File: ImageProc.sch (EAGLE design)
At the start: 96 parts, among them IC1 XC61GC3002HR-G, IC2 MIC5335-SPYMT, IC3 LTC6087, IC4 LTC6087, IC5 AT86RF233-ZU, IC7 DRV8833RTY, IC8 DRV8833RTY, IC9 MPU-6000, J1 CON-HRS-DM3AT, P1 BAT+, P10 MD2, P2 BAT-, P3 MA1, P4 MA2, P5 MB1, P6 MB2, P7 MC1, P8 MC2, P9 MD1, U1 CY8C5688LTI-LP086, U2 SIT8008AI-72-33E-24.000000G

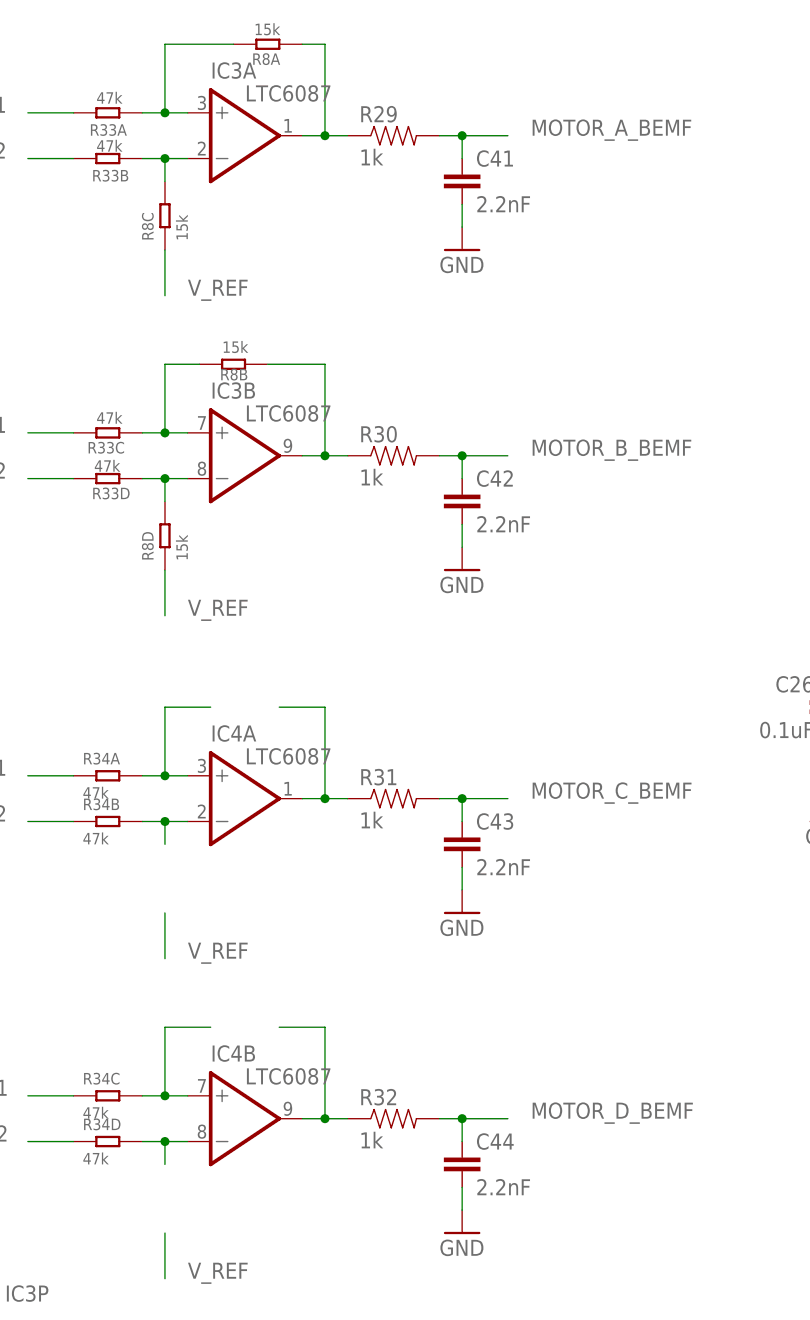
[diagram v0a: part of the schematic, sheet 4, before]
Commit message: Further routing. Moved 1K resistors to res array.
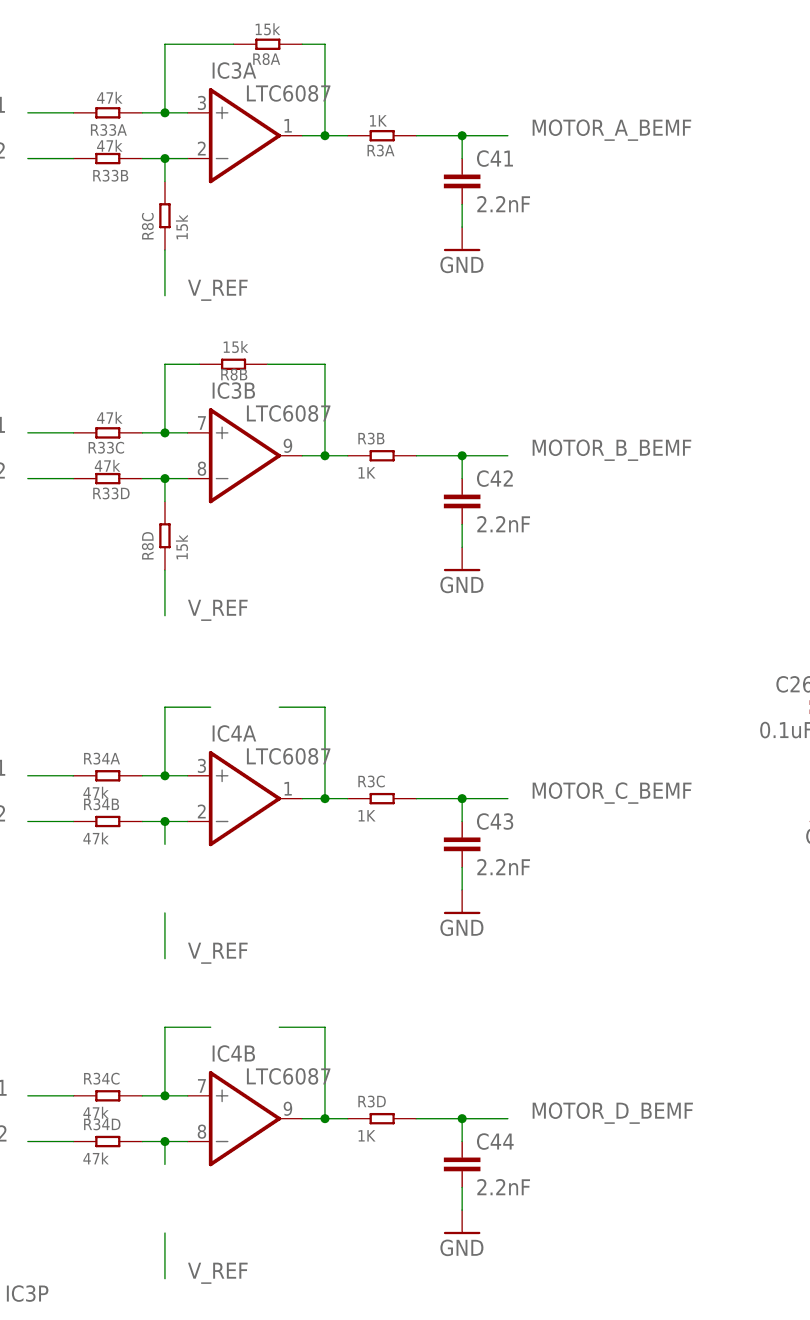
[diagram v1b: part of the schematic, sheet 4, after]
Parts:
- removed R29, R30, R31, R32: 1k, biomimetic:RESISTOR0402-RES
- added R3: 1K, OPL Eagle Library:R-4R
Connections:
- removed net N$21: R4.1, U1G$6.SCL1
- net MOTOR_A_BEMF: now also R3A.2; no longer R29.2
- net MOTOR_B_BEMF: now also R3B.2; no longer R30.2
- net MOTOR_C_BEMF: now also R3C.2; no longer R31.2
- net MOTOR_D_BEMF: now also R3D.2; no longer R32.2
- net N$34: now also R3D.1; no longer R32.1
- net N$35: now also R3C.1; no longer R31.1
- net N$36: now also R3A.1; no longer R29.1
- net N$37: now also R3B.1; no longer R30.1
- net SCL1: now also R4.1, U1G$6.SCL1
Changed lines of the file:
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@@
 <part name="C26" library="biomimetic" deviceset="CAP" device="0402-CAP" value="0.1uF"/>
 <part name="C41" library="biomimetic" deviceset="CAP" device="0402-CAP" value="2.2nF"/>
-<part name="R29" library="biomimetic" deviceset="RESISTOR" device="0402-RES" value="1k"/>
 <part name="C42" library="biomimetic" deviceset="CAP" device="0402-CAP" value="2.2nF"/>
-<part name="R30" library="biomimetic" deviceset="RESISTOR" device="0402-RES" value="1k"/>
 <part name="C43" library="biomimetic" deviceset="CAP" device="0402-CAP" value="2.2nF"/>
-<part name="R31" library="biomimetic" deviceset="RESISTOR" device="0402-RES" value="1k"/>
 <part name="C44" library="biomimetic" deviceset="CAP" device="0402-CAP" value="2.2nF"/>
-<part name="R32" library="biomimetic" deviceset="RESISTOR" device="0402-RES" value="1k"/>
 <part name="GND20" library="biomimetic" deviceset="GND" device=""/>
 <part name="GND26" library="biomimetic" deviceset="GND" device=""/>
@@
 <part name="C40" library="biomimetic" deviceset="CAP" device="0402-CAP" value="1.0uF"/>
 <part name="GND11" library="supply1" deviceset="GND" device=""/>
-<part name="P+10" library="biomimetic" deviceset="3.3V" device=""/>
-<part name="P+5" library="biomimetic" deviceset="3.3V" device=""/>
-<part name="P+7" library="biomimetic" deviceset="3.3V" device=""/>
 <part name="D1" library="diode" deviceset="DIODE-" device="SOD123"/>
 <part name="L1" library="pullin" deviceset="SRN3015-100M" device="" value="10uH"/>
@@
 <part name="GND12" library="supply1" deviceset="GND" device=""/>
 <part name="GND19" library="supply1" deviceset="GND" device=""/>
+<part name="P+5" library="biomimetic" deviceset="3.3V" device=""/>
+<part name="P+7" library="biomimetic" deviceset="3.3V" device=""/>
+<part name="P+10" library="biomimetic" deviceset="3.3V" device=""/>
+<part name="R3" library="OPL Eagle Library" deviceset="R-4R*" device="" value="1K"/>
 </parts>
 <sheets>
@@
 <instance part="C40" gate="G$1" x="119.38" y="22.86"/>
 <instance part="GND11" gate="1" x="101.6" y="55.88"/>
-<instance part="P+10" gate="G$1" x="60.96" y="66.04"/>
-<instance part="P+5" gate="G$1" x="68.58" y="66.04"/>
-<instance part="P+7" gate="G$1" x="76.2" y="66.04"/>
 <instance part="U2" gate="G$1" x="193.04" y="162.56"/>
 <instance part="C48" gate="G$1" x="210.82" y="162.56" rot="MR0">
@@
 <instance part="P+9" gate="G$1" x="175.26" y="170.18"/>
 <instance part="GND12" gate="1" x="167.64" y="154.94"/>
+<instance part="P+5" gate="G$1" x="76.2" y="66.04"/>
+<instance part="P+7" gate="G$1" x="68.58" y="66.04"/>
+<instance part="P+10" gate="G$1" x="60.96" y="66.04"/>
 </instances>
 <busses>
@@
 <wire x1="66.04" y1="162.56" x2="68.58" y2="162.56" width="0.1524" layer="91"/>
 <junction x="66.04" y="170.18"/>
-</segment>
-<segment>
-<wire x1="60.96" y1="66.04" x2="60.96" y2="55.88" width="0.1524" layer="91"/>
-<pinref part="P+10" gate="G$1" pin="3.3V"/>
-</segment>
-<segment>
-<wire x1="68.58" y1="66.04" x2="68.58" y2="55.88" width="0.1524" layer="91"/>
-<pinref part="P+5" gate="G$1" pin="3.3V"/>
-</segment>
-<segment>
-<wire x1="76.2" y1="66.04" x2="76.2" y2="55.88" width="0.1524" layer="91"/>
-<pinref part="P+7" gate="G$1" pin="3.3V"/>
 </segment>
 <segment>
@@
 <wire x1="167.64" y1="165.1" x2="175.26" y2="165.1" width="0.1524" layer="91"/>
 <junction x="175.26" y="165.1"/>
+</segment>
+<segment>
+<wire x1="76.2" y1="55.88" x2="76.2" y2="66.04" width="0.1524" layer="91"/>
+<pinref part="P+5" gate="G$1" pin="3.3V"/>
+</segment>
+<segment>
+<wire x1="68.58" y1="55.88" x2="68.58" y2="66.04" width="0.1524" layer="91"/>
+<pinref part="P+7" gate="G$1" pin="3.3V"/>
+</segment>
+<segment>
+<wire x1="60.96" y1="55.88" x2="60.96" y2="66.04" width="0.1524" layer="91"/>
+<pinref part="P+10" gate="G$1" pin="3.3V"/>
 </segment>
 </net>
@@
 </segment>
 </net>
-<net name="N$21" class="0">
+<net name="SCL1" class="0">
 <segment>
 <pinref part="R4" gate="G$1" pin="1"/>
@@
 <instance part="C26" gate="G$1" x="220.98" y="104.14" rot="MR0"/>
 <instance part="C41" gate="G$1" x="180.34" y="162.56"/>
-<instance part="R29" gate="G$1" x="172.72" y="167.64"/>
 <instance part="C42" gate="G$1" x="180.34" y="127"/>
-<instance part="R30" gate="G$1" x="172.72" y="132.08"/>
 <instance part="C43" gate="G$1" x="180.34" y="88.9"/>
-<instance part="R31" gate="G$1" x="172.72" y="93.98"/>
 <instance part="C44" gate="G$1" x="180.34" y="53.34"/>
-<instance part="R32" gate="G$1" x="172.72" y="58.42"/>
 <instance part="GND20" gate="1" x="180.34" y="81.28"/>
 <instance part="GND26" gate="1" x="180.34" y="154.94"/>
@@
 <instance part="R8" gate="C" x="147.32" y="158.75" rot="R90"/>
 <instance part="R8" gate="D" x="147.32" y="123.19" rot="R90"/>
+<instance part="R3" gate="A" x="171.45" y="167.64" smashed="yes">
+<attribute name="NAME" x="169.672" y="165.354" size="1.27" layer="95" ratio="10"/>
+<attribute name="VALUE" x="169.926" y="168.656" size="1.27" layer="96" ratio="10"/>
+</instance>
+<instance part="R3" gate="B" x="171.45" y="132.08"/>
+<instance part="R3" gate="C" x="171.45" y="93.98"/>
+<instance part="R3" gate="D" x="171.45" y="58.42"/>
 </instances>
 <busses>
@@
 <net name="MOTOR_D_BEMF" class="0">
 <segment>
-<pinref part="R32" gate="G$1" pin="2"/>
 <label x="187.96" y="58.42" size="1.778" layer="95"/>
-<wire x1="177.8" y1="58.42" x2="180.34" y2="58.42" width="0.1524" layer="91"/>
+<wire x1="175.26" y1="58.42" x2="180.34" y2="58.42" width="0.1524" layer="91"/>
 <pinref part="C44" gate="G$1" pin="1"/>
 <wire x1="180.34" y1="58.42" x2="185.42" y2="58.42" width="0.1524" layer="91"/>
 <wire x1="180.34" y1="55.88" x2="180.34" y2="58.42" width="0.1524" layer="91"/>
 <junction x="180.34" y="58.42"/>
+<pinref part="R3" gate="D" pin="2"/>
 </segment>
 </net>
@@
 <net name="N$34" class="0">
 <segment>
-<pinref part="R32" gate="G$1" pin="1"/>
 <wire x1="162.56" y1="58.42" x2="165.1" y2="58.42" width="0.1524" layer="91"/>
 <wire x1="165.1" y1="58.42" x2="167.64" y2="58.42" width="0.1524" layer="91"/>
@@
 <junction x="165.1" y="58.42"/>
 <pinref part="IC4" gate="B" pin="OUT"/>
+<pinref part="R3" gate="D" pin="1"/>
 </segment>
 </net>
@@
 <wire x1="160.02" y1="104.14" x2="165.1" y2="104.14" width="0.1524" layer="91"/>
 <wire x1="165.1" y1="104.14" x2="165.1" y2="93.98" width="0.1524" layer="91"/>
-<pinref part="R31" gate="G$1" pin="1"/>
 <wire x1="165.1" y1="93.98" x2="167.64" y2="93.98" width="0.1524" layer="91"/>
 <junction x="165.1" y="93.98"/>
 <pinref part="IC4" gate="A" pin="OUT"/>
+<pinref part="R3" gate="C" pin="1"/>
 </segment>
 </net>
@@
 <wire x1="180.34" y1="93.98" x2="185.42" y2="93.98" width="0.1524" layer="91"/>
 <wire x1="180.34" y1="91.44" x2="180.34" y2="93.98" width="0.1524" layer="91"/>
-<pinref part="R31" gate="G$1" pin="2"/>
-<wire x1="177.8" y1="93.98" x2="180.34" y2="93.98" width="0.1524" layer="91"/>
+<wire x1="175.26" y1="93.98" x2="180.34" y2="93.98" width="0.1524" layer="91"/>
 <junction x="180.34" y="93.98"/>
 <label x="187.96" y="93.98" size="1.778" layer="95"/>
+<pinref part="R3" gate="C" pin="2"/>
 </segment>
 </net>
 <net name="N$37" class="0">
 <segment>
-<pinref part="R30" gate="G$1" pin="1"/>
 <wire x1="162.56" y1="132.08" x2="165.1" y2="132.08" width="0.1524" layer="91"/>
 <wire x1="165.1" y1="132.08" x2="167.64" y2="132.08" width="0.1524" layer="91"/>
@@
 <pinref part="R8" gate="B" pin="2"/>
 <pinref part="IC3" gate="B" pin="OUT"/>
+<pinref part="R3" gate="B" pin="1"/>
 </segment>
 </net>
 <net name="MOTOR_B_BEMF" class="0">
 <segment>
-<pinref part="R30" gate="G$1" pin="2"/>
-<wire x1="177.8" y1="132.08" x2="180.34" y2="132.08" width="0.1524" layer="91"/>
+<wire x1="175.26" y1="132.08" x2="180.34" y2="132.08" width="0.1524" layer="91"/>
 <pinref part="C42" gate="G$1" pin="1"/>
 <wire x1="180.34" y1="132.08" x2="185.42" y2="132.08" width="0.1524" layer="91"/>
@@
 <junction x="180.34" y="132.08"/>
 <label x="187.96" y="132.08" size="1.778" layer="95"/>
+<pinref part="R3" gate="B" pin="2"/>
 </segment>
 </net>
 <net name="N$36" class="0">
 <segment>
-<pinref part="R29" gate="G$1" pin="1"/>
 <wire x1="162.56" y1="167.64" x2="165.1" y2="167.64" width="0.1524" layer="91"/>
 <wire x1="165.1" y1="167.64" x2="167.64" y2="167.64" width="0.1524" layer="91"/>
@@
 <pinref part="R8" gate="A" pin="2"/>
 <pinref part="IC3" gate="A" pin="OUT"/>
+<pinref part="R3" gate="A" pin="1"/>
 </segment>
 </net>
 <net name="MOTOR_A_BEMF" class="0">
 <segment>
-<pinref part="R29" gate="G$1" pin="2"/>
-<wire x1="177.8" y1="167.64" x2="180.34" y2="167.64" width="0.1524" layer="91"/>
+<wire x1="175.26" y1="167.64" x2="180.34" y2="167.64" width="0.1524" layer="91"/>
 <pinref part="C41" gate="G$1" pin="1"/>
 <wire x1="180.34" y1="167.64" x2="185.42" y2="167.64" width="0.1524" layer="91"/>
@@
 <junction x="180.34" y="167.64"/>
 <label x="187.96" y="167.64" size="1.778" layer="95"/>
-</segment>
-</net>
+<pinref part="R3" gate="A" pin="2"/>
+</segment>
+</net>

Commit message: More routing done. Many voltage domains merged to 3.3v and GND.
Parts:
- removed C49: 15pF, biomimetic:CAP0402-CAP
- added LED4: YELLOW, biomimetic:LED0603
- added R6, R7: 2K, biomimetic:RESISTOR0402-RES
- added U$4: MCP73831, pullin:MCP73831
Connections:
- net U2RX renamed U1RX
- net U2TX renamed U1TX
- net VBAT renamed V_BOOSTED_4.2V
- removed net N$33: JP6.VBUS
- removed net VDDA: C11.1, C13.1, U1G$7.VDDA
- removed net VDDD: C10.1, C12.1, C15.1, C2.1, C36.1, C45.1, C46.1, C5.1, C8.1, D1.C, U1G$7.VDDD, U1G$7.VDDD2, U1G$7.VDDIO0, U1G$7.VDDIO1, U1G$7.VDDIO2, U1G$7.VDDIO3
- removed net VSSD: C10.2, C12.2, C15.2, C2.2, C36.2, C40.2, C5.2, C8.2, U1G$7.VSSD_PAD
- new net 5V_USB: JP6.VBUS, LED4.A, U$4.VDD
- new net N$11: LED4.C, R7.1
- new net N$21: R7.2, U$4.STAT
- new net N$5: R6.1, U$4.PROG
- net 24MHZ: now also U2.OUT
- net 3.3V: now also C10.1, C11.1, C12.1, C13.1, C15.1, C2.1, C36.1, C45.1, C46.1, C5.1, C8.1, D1.C, U1G$7.VDDA, U1G$7.VDDD, U1G$7.VDDD2, U1G$7.VDDIO0, U1G$7.VDDIO1, U1G$7.VDDIO2, U1G$7.VDDIO3; no longer C49.1
- net GND: now also C10.2, C11.2, C12.2, C14.2, C15.2, C2.2, C36.2, C40.2, C45.2, C46.2, C5.2, C8.2, R6.2, U$4.EP, U$4.VSS, U1G$7.VSSA, U1G$7.VSSD_PAD; no longer C49.2
- net MOTOR_A_IN1: no longer IC7S.AIN1
- net MOTOR_A_IN2: no longer IC7S.AIN2
- net MOTOR_A_OUT1: no longer R33A.1
- net MOTOR_A_OUT2: no longer R33B.1
- net MOTOR_B_IN1: no longer IC7S.BIN1
- net MOTOR_B_IN2: no longer IC7S.BIN2
- net MOTOR_B_OUT1: no longer R33C.1
- net MOTOR_B_OUT2: no longer R33D.1
- net MOTOR_C_IN1: no longer IC8S.AIN1
- net MOTOR_C_IN2: no longer IC8S.AIN2
- net MOTOR_C_OUT1: no longer R34A.1
- net MOTOR_C_OUT2: no longer R34B.1
- net MOTOR_D_IN1: no longer IC8S.BIN1
- net MOTOR_D_IN2: no longer IC8S.BIN2
- net MOTOR_D_OUT1: no longer R34C.1
- net MOTOR_D_OUT2: no longer R34D.1
- net VSSA: no longer C11.2, C14.2, C45.2, C46.2, U1G$7.VSSA
- net V_BATT: now also U$4.VBAT
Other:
- note added: "Charger"
- note added: "VCCA"
- note added: "VSSBOOST"
- moved on the sheet: C45, C46, C9, D1, L1

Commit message: More routing. Starting to use rough paths just to set topology.
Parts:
- removed C29: 0.1uF, biomimetic:CAP0402-CAP
- removed IC4: LTC6087, biomimetic:LTC6087
- removed R33, R34: 47k, OPL Eagle Library:R-4R
- added R10, R11, R9: 1K, biomimetic:RESISTOR0402-RES
- added R12, R13, R14, R15, R16, R17, R18: 15K, biomimetic:RESISTOR0402-RES
- added R19, R20, R21, R22, R23, R24, R25, R29: 47k, biomimetic:RESISTOR0402-RES
- IC3: value LTC6087 -> LTC6088; device biomimetic:LTC6087 -> biomimetic:LTC6088
- R3: device OPL Eagle Library:R-4R -> biomimetic:RESISTOR0402-RES
- R8: value 15k -> 15K; device OPL Eagle Library:R-4R -> biomimetic:RESISTOR0402-RES
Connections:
- new net RADIO_!RST: IC5S.!RST, U1G$4.RADIO_!RST
- net !XRES: no longer IC5S.!RST
- net 3.3V: no longer C29.1, IC4P.V+
- net GND: no longer C29.2, IC4P.V-
- net MOTOR_A_BEMF: now also R3.1; no longer R3A.2
- net MOTOR_A_IN1: now also IC7S.AIN1
- net MOTOR_A_IN2: now also IC7S.AIN2
- net MOTOR_A_OUT1: now also R29.2
- net MOTOR_A_OUT2: now also R25.2
- net MOTOR_B_BEMF: now also R9.1; no longer R3B.2
- net MOTOR_B_IN1: now also IC7S.BIN1
- net MOTOR_B_IN2: now also IC7S.BIN2
- net MOTOR_B_OUT1: now also R23.2
- net MOTOR_B_OUT2: now also R24.2
- net MOTOR_C_BEMF: now also R10.1; no longer R3C.2
- net MOTOR_C_IN1: now also IC8S.AIN1
- net MOTOR_C_IN2: now also IC8S.AIN2
- net MOTOR_C_OUT1: now also R22.2
- net MOTOR_C_OUT2: now also R21.2
- net MOTOR_D_BEMF: now also R11.1; no longer R3D.2
- net MOTOR_D_IN1: now also IC8S.BIN1
- net MOTOR_D_IN2: now also IC8S.BIN2
- net MOTOR_D_OUT1: now also R20.2
- net MOTOR_D_OUT2: now also R19.2
- net N$22: now also IC3D.+IN, R13.2, R24.1; no longer IC3B.+IN, R33C.2, R8B.1
- net N$23: now also IC3D.-IN, R16.1, R23.1; no longer IC3B.-IN, R33D.2, R8D.2
- net N$24: now also IC3A.+IN, R14.2, R22.1; no longer IC4A.+IN, R34A.2
- net N$25: now also IC3A.-IN, R17.1, R21.1; no longer IC4A.-IN, R34B.2
- net N$26: now also IC3B.+IN, R15.2, R20.1; no longer IC4B.+IN, R34C.2
- net N$27: now also IC3B.-IN, R18.1, R19.1; no longer IC4B.-IN, R34D.2
- net N$30: now also IC3C.+IN, R12.2, R29.1; no longer IC3A.+IN, R33A.2, R8A.1
- net N$31: now also IC3C.-IN, R25.1, R8.1; no longer IC3A.-IN, R33B.2, R8C.2
- net N$34: now also IC3B.OUT, R11.2, R15.1; no longer IC4B.OUT, R3D.1
- net N$35: now also IC3A.OUT, R10.2, R14.1; no longer IC4A.OUT, R3C.1
- net N$36: now also IC3C.OUT, R12.1, R3.2; no longer IC3A.OUT, R3A.1, R8A.2
- net N$37: now also IC3D.OUT, R13.1, R9.2; no longer IC3B.OUT, R3B.1, R8B.2
- net SWD_SCLK: now also JP1.5; no longer JP1.4
- net SWD_SDAT: now also JP1.4; no longer JP1.5
- net V_REF: now also R16.2, R17.2, R18.2, R8.2, U1G$1.VREF_OUT; no longer R8C.1, R8D.1
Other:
- moved on the sheet: IC3A, IC3B, IC3P
